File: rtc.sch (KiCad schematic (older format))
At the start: 16 parts, among them U36 74LS05, U9 MSM6242B, Y9 32768 Hz

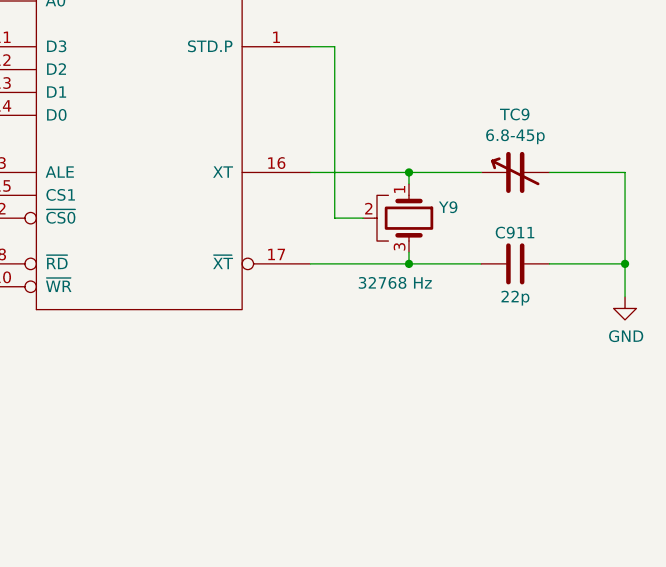
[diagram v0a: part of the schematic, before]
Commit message: Add RTC crystal frequency on silkscreen
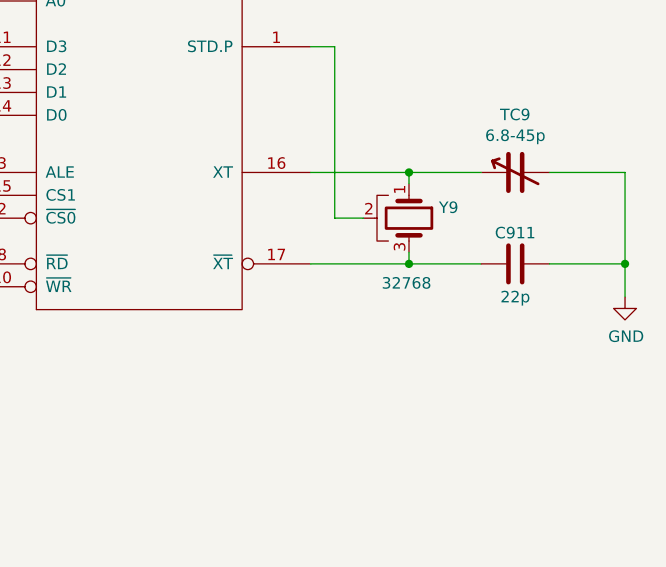
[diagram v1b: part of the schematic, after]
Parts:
- Y9: value 32768 Hz -> 32768
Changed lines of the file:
@@
 Sheet 13 14
 Title "Rämixx500"
-Date "2019-04-23"
+Date "2021-05-23"
 Rev "1"
 Comp "SukkoPera"
@@
 P 9175 2525
 F 0 "Y9" V 9129 2656 50  0000 L CNN
-F 1 "32768 Hz" V 9460 2300 50  0000 L CNN
+F 1 "32768" V 9460 2405 50  0000 L CNN
 F 2 "Raemixx500:Crystal_RTC" H 9175 2525 50  0001 C CNN
 F 3 "~" H 9175 2525 50  0001 C CNN
